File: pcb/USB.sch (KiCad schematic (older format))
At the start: 9 parts

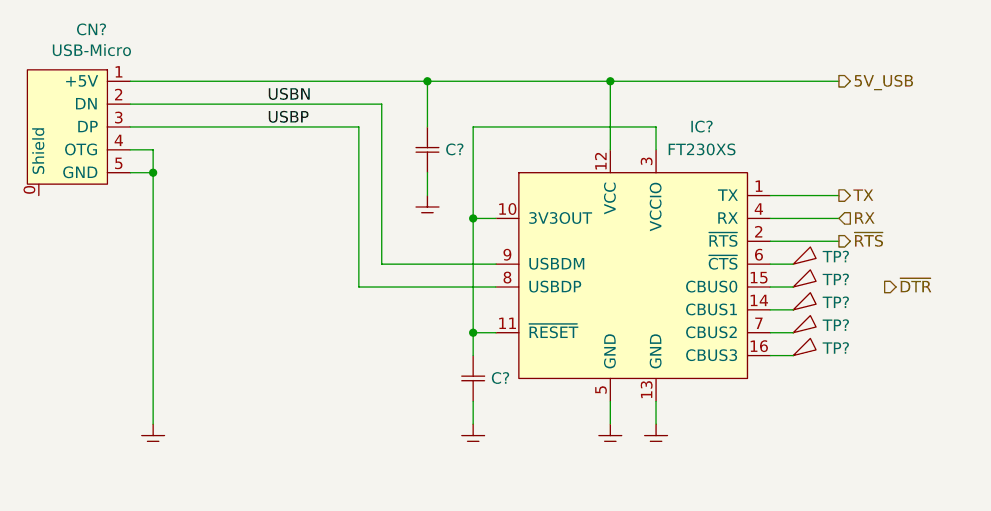
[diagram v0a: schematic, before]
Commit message: changed serial adapter to ch340
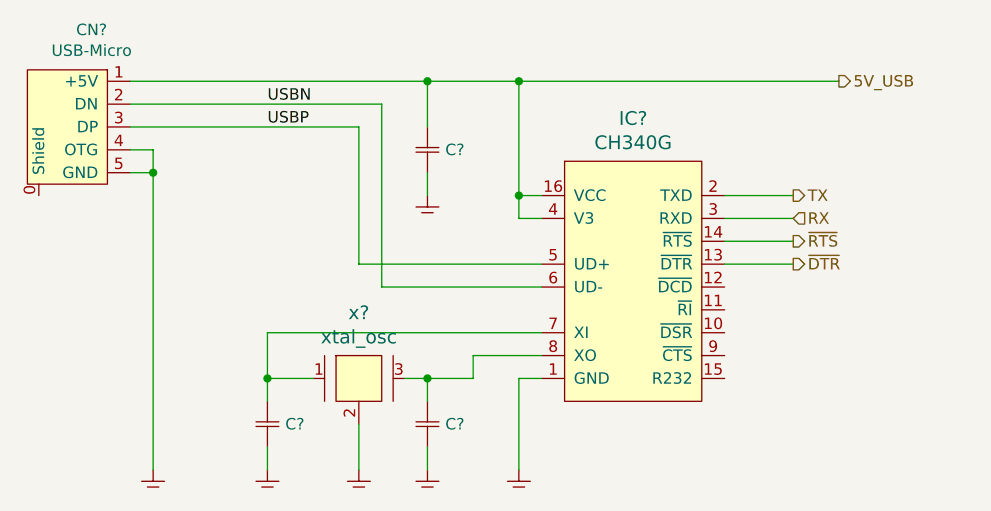
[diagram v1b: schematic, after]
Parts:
- removed C?: C, SMT:0603, symbol generic:C
- removed IC?: FT230XS, SSOP:SSOP-16, symbol serial:FT230XS
- removed TP? (x5): test_point, PCB:test_point, symbol PCB:test_point
- added C? (x2): C, SMT:0603, symbol generic:C
- added IC?: CH340G, symbol serial:CH340G
- added x?: xtal_osc, symbol oscillators:xtal_osc
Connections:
- net 5V_USB: now also IC?.16 (VCC), IC?.4 (V3)
- net GND: now also C?.2, C?.2, IC?.1 (GND), x?.2, x?.4
- net RX: now also IC?.3 (RXD)
- net TX: now also IC?.2 (TXD)
- net USBN: now also IC?.6 (UD-)
- net USBP: now also IC?.5 (UD+)
- net ~DTR: now also IC?.13 (~DTR)
- net ~RTS: now also IC?.14 (~RTS)
- new net: C?.1, IC?.7 (XI), x?.1
- new net: C?.1, IC?.8 (XO), x?.3
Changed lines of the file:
@@
 L generic:GND #GND?
 U 1 1 5D45B32E
-P 4200 4900
-F 0 "#GND?" H 4350 4950 50  0001 C CNN
-F 1 "GND" H 4350 4900 50  0001 C CNN
-F 2 "" H 4200 4900 50  0001 C CNN
-F 3 "" H 4200 4900 50  0001 C CNN
-	1    4200 4900
+P 4200 5100
+F 0 "#GND?" H 4350 5150 50  0001 C CNN
+F 1 "GND" H 4350 5100 50  0001 C CNN
+F 2 "" H 4200 5100 50  0001 C CNN
+F 3 "" H 4200 5100 50  0001 C CNN
+	1    4200 5100
 	1    0    0    -1
 $EndComp
@@
 	4100 3800 4200 3800
 Wire Wire Line
-	4200 3800 4200 4900
-Text HLabel 7200 3900 2    50   Output ~ 0
+	4200 3800 4200 5100
+Text HLabel 7000 3900 2    50   Output ~ 0
 TX
-Text HLabel 7200 4000 2    50   Input ~ 0
+Text HLabel 7000 4000 2    50   Input ~ 0
 RX
 Wire Wire Line
@@
 Connection ~ 4200 3800
 $Comp
-L serial:FT230XS IC?
-U 1 1 5D83DBBB
-P 6300 4200
-F 0 "IC?" H 6600 4800 50  0000 C CNN
-F 1 "FT230XS" H 6600 4700 50  0000 C CNN
-F 2 "SSOP:SSOP-16" H 6300 4200 50  0001 C CNN
-F 3 "" H 6300 4200 50  0001 C CNN
-	1    6300 4200
-	1    0    0    -1
-$EndComp
-$Comp
-L generic:GND #GND?
-U 1 1 5D83DE64
-P 6200 4900
-F 0 "#GND?" H 6350 4950 50  0001 C CNN
-F 1 "GND" H 6350 4900 50  0001 C CNN
-F 2 "" H 6200 4900 50  0001 C CNN
-F 3 "" H 6200 4900 50  0001 C CNN
-	1    6200 4900
-	1    0    0    -1
-$EndComp
-$Comp
-L generic:GND #GND?
-U 1 1 5D83DE77
-P 6400 4900
-F 0 "#GND?" H 6550 4950 50  0001 C CNN
-F 1 "GND" H 6550 4900 50  0001 C CNN
-F 2 "" H 6400 4900 50  0001 C CNN
-F 3 "" H 6400 4900 50  0001 C CNN
-	1    6400 4900
-	1    0    0    -1
-$EndComp
-Wire Wire Line
-	6400 4800 6400 4900
-Wire Wire Line
-	6200 4900 6200 4800
-Wire Wire Line
-	5700 4000 5600 4000
-Wire Wire Line
-	5600 4000 5600 3600
-Wire Wire Line
-	5600 3600 6400 3600
-Wire Wire Line
-	6400 3600 6400 3700
-Wire Wire Line
-	6200 3700 6200 3400
-$Comp
-L generic:C C?
-U 1 1 5D83E469
-P 5600 4700
-F 0 "C?" H 5678 4700 50  0000 L CNN
-F 1 "C" H 5700 4600 50  0001 C CNN
-F 2 "SMT:0603" H 5600 4600 50  0001 C CNN
-F 3 "" H 5600 4700 50  0001 C CNN
-	1    5600 4700
-	1    0    0    -1
-$EndComp
-Wire Wire Line
-	5200 3500 5200 4200
-$Comp
 L generic:GND #GND?
 U 1 1 5D83EA0A
-P 5600 4900
-F 0 "#GND?" H 5750 4950 50  0001 C CNN
-F 1 "GND" H 5750 4900 50  0001 C CNN
-F 2 "" H 5600 4900 50  0001 C CNN
-F 3 "" H 5600 4900 50  0001 C CNN
-	1    5600 4900
-	1    0    0    -1
-$EndComp
-Wire Wire Line
-	5600 4800 5600 4900
-Wire Wire Line
-	5600 4600 5600 4500
-Connection ~ 5600 4000
-Wire Wire Line
-	5100 4300 5100 3600
-Wire Wire Line
-	6900 3900 7200 3900
-Wire Wire Line
-	7200 4000 6900 4000
-Wire Wire Line
-	5700 4500 5600 4500
-Connection ~ 5600 4500
-Wire Wire Line
-	5600 4500 5600 4000
+P 5800 5100
+F 0 "#GND?" H 5950 5150 50  0001 C CNN
+F 1 "GND" H 5950 5100 50  0001 C CNN
+F 2 "" H 5800 5100 50  0001 C CNN
+F 3 "" H 5800 5100 50  0001 C CNN
+	1    5800 5100
+	1    0    0    -1
+$EndComp
 $Comp
 L generic:C C?
@@
 	1    0    0    -1
 $EndComp
-Connection ~ 6200 3400
-Wire Wire Line
-	6200 3400 7200 3400
-Wire Wire Line
-	5100 4300 5700 4300
-Wire Wire Line
-	5200 4200 5700 4200
 Wire Wire Line
 	5400 3900 5400 3800
 Wire Wire Line
 	5400 3600 5400 3400
-Wire Wire Line
-	5400 3400 6200 3400
 Wire Wire Line
 	4100 3600 5100 3600
@@
 	4100 3500 5200 3500
 Connection ~ 5400 3400
-$Comp
-L PCB:test_point TP?
-U 1 1 5D846BB7
-P 7000 4300
-F 0 "TP?" H 7129 4331 50  0000 L CNN
-F 1 "test_point" H 7000 4400 50  0001 C CNN
-F 2 "PCB:test_point" H 7100 4250 50  0001 C CNN
-F 3 "" H 7000 4300 50  0001 C CNN
-	1    7000 4300
-	1    0    0    -1
-$EndComp
-$Comp
-L PCB:test_point TP?
-U 1 1 5D846BF3
-P 7000 4400
-F 0 "TP?" H 7129 4431 50  0000 L CNN
-F 1 "test_point" H 7000 4500 50  0001 C CNN
-F 2 "PCB:test_point" H 7100 4350 50  0001 C CNN
-F 3 "" H 7000 4400 50  0001 C CNN
-	1    7000 4400
-	1    0    0    -1
-$EndComp
-$Comp
-L PCB:test_point TP?
-U 1 1 5D846C11
-P 7000 4500
-F 0 "TP?" H 7129 4531 50  0000 L CNN
-F 1 "test_point" H 7000 4600 50  0001 C CNN
-F 2 "PCB:test_point" H 7100 4450 50  0001 C CNN
-F 3 "" H 7000 4500 50  0001 C CNN
-	1    7000 4500
-	1    0    0    -1
-$EndComp
-$Comp
-L PCB:test_point TP?
-U 1 1 5D846C31
-P 7000 4600
-F 0 "TP?" H 7129 4631 50  0000 L CNN
-F 1 "test_point" H 7000 4700 50  0001 C CNN
-F 2 "PCB:test_point" H 7100 4550 50  0001 C CNN
-F 3 "" H 7000 4600 50  0001 C CNN
-	1    7000 4600
-	1    0    0    -1
-$EndComp
-Wire Wire Line
-	7000 4600 6900 4600
-Wire Wire Line
-	6900 4500 7000 4500
-Wire Wire Line
-	7000 4400 6900 4400
-Wire Wire Line
-	6900 4300 7000 4300
-$Comp
-L PCB:test_point TP?
-U 1 1 5D848267
-P 7000 4200
-F 0 "TP?" H 7129 4231 50  0000 L CNN
-F 1 "test_point" H 7000 4300 50  0001 C CNN
-F 2 "PCB:test_point" H 7100 4150 50  0001 C CNN
-F 3 "" H 7000 4200 50  0001 C CNN
-	1    7000 4200
-	1    0    0    -1
-$EndComp
-Wire Wire Line
-	7000 4200 6900 4200
 Text Label 4700 3500 0    50   ~ 0
 USBN
@@
 Wire Wire Line
 	4100 3400 5400 3400
-Text HLabel 7400 4300 2    50   Output ~ 0
+Text HLabel 7000 4200 2    50   Output ~ 0
 ~DTR
-Text HLabel 7200 4100 2    50   Output ~ 0
+Text HLabel 7000 4100 2    50   Output ~ 0
 ~RTS
-Wire Wire Line
-	6900 4100 7200 4100
+$Comp
+L serial:CH340G IC?
+U 1 1 5EC98B45
+P 6300 4300
+F 0 "IC?" H 6300 5037 60  0000 C CNN
+F 1 "CH340G" H 6300 4931 60  0000 C CNN
+F 2 "" H 6300 4300 60  0000 C CNN
+F 3 "" H 6300 4300 60  0000 C CNN
+	1    6300 4300
+	1    0    0    -1
+$EndComp
+Wire Wire Line
+	5400 3400 5800 3400
+Wire Wire Line
+	5900 4000 5800 4000
+Wire Wire Line
+	5800 4000 5800 3900
+Connection ~ 5800 3400
+Wire Wire Line
+	5800 3400 7200 3400
+Wire Wire Line
+	5900 3900 5800 3900
+Connection ~ 5800 3900
+Wire Wire Line
+	5800 3900 5800 3400
+Wire Wire Line
+	5900 4700 5800 4700
+Wire Wire Line
+	5800 4700 5800 5100
+Wire Wire Line
+	7000 4200 6700 4200
+Wire Wire Line
+	6700 4100 7000 4100
+Wire Wire Line
+	6700 4000 7000 4000
+Wire Wire Line
+	6700 3900 7000 3900
+Wire Wire Line
+	5200 3500 5200 4300
+Wire Wire Line
+	5900 4300 5200 4300
+Wire Wire Line
+	5900 4200 5100 4200
+Wire Wire Line
+	5100 4200 5100 3600
+$Comp
+L oscillators:xtal_osc x?
+U 1 1 5EC9BB62
+P 5100 4700
+F 0 "x?" H 5100 4987 60  0000 C CNN
+F 1 "xtal_osc" H 5100 4881 60  0000 C CNN
+F 2 "" H 5100 4750 60  0000 C CNN
+F 3 "" H 5100 4750 60  0000 C CNN
+	1    5100 4700
+	1    0    0    -1
+$EndComp
+$Comp
+L generic:GND #GND?
+U 1 1 5EC9BE0B
+P 5100 5100
+F 0 "#GND?" H 5250 5150 50  0001 C CNN
+F 1 "GND" H 5250 5100 50  0001 C CNN
+F 2 "" H 5100 5100 50  0001 C CNN
+F 3 "" H 5100 5100 50  0001 C CNN
+	1    5100 5100
+	1    0    0    -1
+$EndComp
+Wire Wire Line
+	5100 4900 5100 5100
+Wire Wire Line
+	5300 4700 5400 4700
+Wire Wire Line
+	5600 4700 5600 4600
+Wire Wire Line
+	5600 4600 5900 4600
+Wire Wire Line
+	5900 4500 4700 4500
+Wire Wire Line
+	4700 4500 4700 4700
+Wire Wire Line
+	4700 4700 4900 4700
+$Comp
+L generic:C C?
+U 1 1 5EC9D8A3
+P 5400 4900
+F 0 "C?" H 5478 4900 50  0000 L CNN
+F 1 "C" H 5500 4800 50  0001 C CNN
+F 2 "SMT:0603" H 5400 4800 50  0001 C CNN
+F 3 "" H 5400 4900 50  0001 C CNN
+	1    5400 4900
+	1    0    0    -1
+$EndComp
+$Comp
+L generic:C C?
+U 1 1 5EC9D8C7
+P 4700 4900
+F 0 "C?" H 4778 4900 50  0000 L CNN
+F 1 "C" H 4800 4800 50  0001 C CNN
+F 2 "SMT:0603" H 4700 4800 50  0001 C CNN
+F 3 "" H 4700 4900 50  0001 C CNN
+	1    4700 4900
+	1    0    0    -1
+$EndComp
+$Comp
+L generic:GND #GND?
+U 1 1 5EC9DD62
+P 5400 5100
+F 0 "#GND?" H 5550 5150 50  0001 C CNN
+F 1 "GND" H 5550 5100 50  0001 C CNN
+F 2 "" H 5400 5100 50  0001 C CNN
+F 3 "" H 5400 5100 50  0001 C CNN
+	1    5400 5100
+	1    0    0    -1
+$EndComp
+$Comp
+L generic:GND #GND?
+U 1 1 5EC9DD79
+P 4700 5100
+F 0 "#GND?" H 4850 5150 50  0001 C CNN
+F 1 "GND" H 4850 5100 50  0001 C CNN
+F 2 "" H 4700 5100 50  0001 C CNN
+F 3 "" H 4700 5100 50  0001 C CNN
+	1    4700 5100
+	1    0    0    -1
+$EndComp
+Wire Wire Line
+	5400 5100 5400 5000
+Wire Wire Line
+	5400 4800 5400 4700
+Connection ~ 5400 4700
+Wire Wire Line
+	5400 4700 5600 4700
+Wire Wire Line
+	4700 4700 4700 4800
+Connection ~ 4700 4700
+Wire Wire Line
+	4700 5000 4700 5100
 $EndSCHEMATC
